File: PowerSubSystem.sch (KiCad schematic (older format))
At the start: 4 parts, among them U3 LM3671

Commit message: i'm about to say fuck it to the pcb. if it doesn't work out. return here
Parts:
- gave numbers to parts that had none: 3
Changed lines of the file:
@@
 PSU_5VIn+
 $Comp
-L Device:C_Small C?
+L Device:C_Small C1
 U 1 1 613D8B5E
 P 4700 3700
-F 0 "C?" H 4500 3750 50  0000 L CNN
+F 0 "C1" H 4500 3750 50  0000 L CNN
 F 1 "4.7uF" H 4400 3650 50  0000 L CNN
 F 2 "Capacitor_SMD:C_0805_2012Metric" H 4700 3700 50  0001 C CNN
@@
 	4900 3650 4900 3950
 $Comp
-L Device:L_Small L?
+L Device:L_Small L1
 U 1 1 613E2221
 P 5900 3450
-F 0 "L?" V 6085 3450 50  0000 C CNN
+F 0 "L1" V 6085 3450 50  0000 C CNN
 F 1 "2.2uH" V 5994 3450 50  0000 C CNN
 F 2 "Inductor_SMD:L_1210_3225Metric" H 5900 3450 50  0001 C CNN
@@
 	4700 4050 4700 3950
 $Comp
-L Device:C_Small C?
+L Device:C_Small C2
 U 1 1 613E66FD
 P 6350 3700
-F 0 "C?" H 6442 3746 50  0000 L CNN
+F 0 "C2" H 6442 3746 50  0000 L CNN
 F 1 "10uF" H 6442 3655 50  0000 L CNN
 F 2 "Capacitor_SMD:C_0805_2012Metric" H 6350 3700 50  0001 C CNN

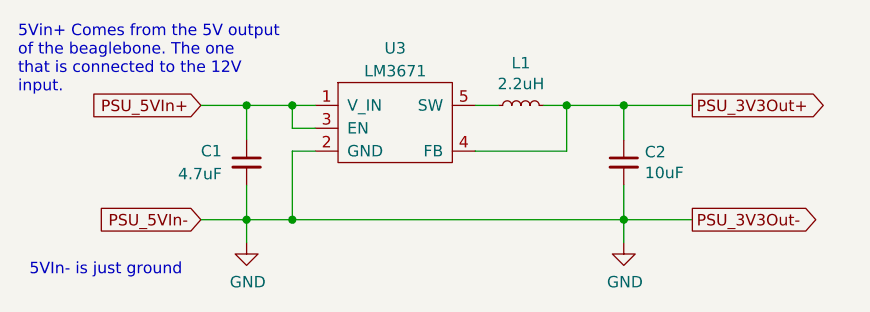
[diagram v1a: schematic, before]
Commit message: part way through getting new ICs and other components back on the PCB
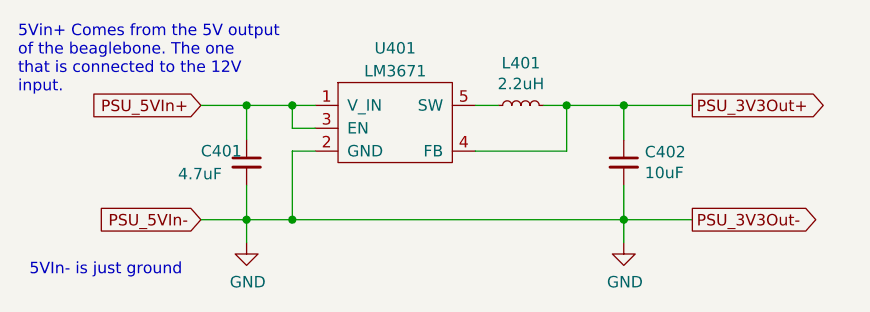
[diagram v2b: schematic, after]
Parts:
- renumbered C1 to C401, C2 to C402, L1 to L401, U3 to U401
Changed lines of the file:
@@
 5Vin+ Comes from the 5V output \nof the beaglebone. The one \nthat is connected to the 12V \ninput.
 $Comp
-L pwr_BeagleBone:LM3671 U3
+L pwr_BeagleBone:LM3671 U401
 U 1 1 613D6B2B
 P 5350 3300
-F 0 "U3" H 5350 3400 50  0000 C CNN
+F 0 "U401" H 5350 3400 50  0000 C CNN
 F 1 "LM3671" H 5350 3300 50  0000 C CNN
 F 2 "Package_TO_SOT_SMD:SOT-23-5" H 5350 3300 50  0001 C CNN
@@
 PSU_5VIn+
 $Comp
-L Device:C_Small C1
+L Device:C_Small C401
 U 1 1 613D8B5E
 P 4700 3700
-F 0 "C1" H 4500 3750 50  0000 L CNN
+F 0 "C401" H 4500 3750 50  0000 L CNN
 F 1 "4.7uF" H 4400 3650 50  0000 L CNN
 F 2 "Capacitor_SMD:C_0805_2012Metric" H 4700 3700 50  0001 C CNN
@@
 	4900 3650 4900 3950
 $Comp
-L Device:L_Small L1
+L Device:L_Small L401
 U 1 1 613E2221
 P 5900 3450
-F 0 "L1" V 6085 3450 50  0000 C CNN
+F 0 "L401" V 6085 3450 50  0000 C CNN
 F 1 "2.2uH" V 5994 3450 50  0000 C CNN
 F 2 "Inductor_SMD:L_1210_3225Metric" H 5900 3450 50  0001 C CNN
@@
 	6100 3650 6100 3450
 $Comp
-L power:GND #PWR0102
+L power:GND #PWR0401
 U 1 1 613E4C24
 P 4700 4050
-F 0 "#PWR0102" H 4700 3800 50  0001 C CNN
+F 0 "#PWR0401" H 4700 3800 50  0001 C CNN
 F 1 "GND" H 4705 3877 50  0000 C CNN
 F 2 "" H 4700 4050 50  0001 C CNN
@@
 	4700 4050 4700 3950
 $Comp
-L Device:C_Small C2
+L Device:C_Small C402
 U 1 1 613E66FD
 P 6350 3700
-F 0 "C2" H 6442 3746 50  0000 L CNN
+F 0 "C402" H 6442 3746 50  0000 L CNN
 F 1 "10uF" H 6442 3655 50  0000 L CNN
 F 2 "Capacitor_SMD:C_0805_2012Metric" H 6350 3700 50  0001 C CNN
@@
 $EndComp
 $Comp
-L power:GND #PWR0109
+L power:GND #PWR0402
 U 1 1 613EB575
 P 6350 4050
-F 0 "#PWR0109" H 6350 3800 50  0001 C CNN
+F 0 "#PWR0402" H 6350 3800 50  0001 C CNN
 F 1 "GND" H 6355 3877 50  0000 C CNN
 F 2 "" H 6350 4050 50  0001 C CNN
